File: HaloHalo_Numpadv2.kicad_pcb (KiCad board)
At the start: 2 copper layers, 112 x 105.4 mm, 92 parts, among them SW1 SW_SPST, SW10 SW_SPST, SW11 SW_SPST, SW12 SW_SPST, SW13 SW_SPST, SW14 SW_SPST, SW15 SW_SPST, SW16 SW_SPST, SW17 SW_SPST, SW18 SW_SPST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

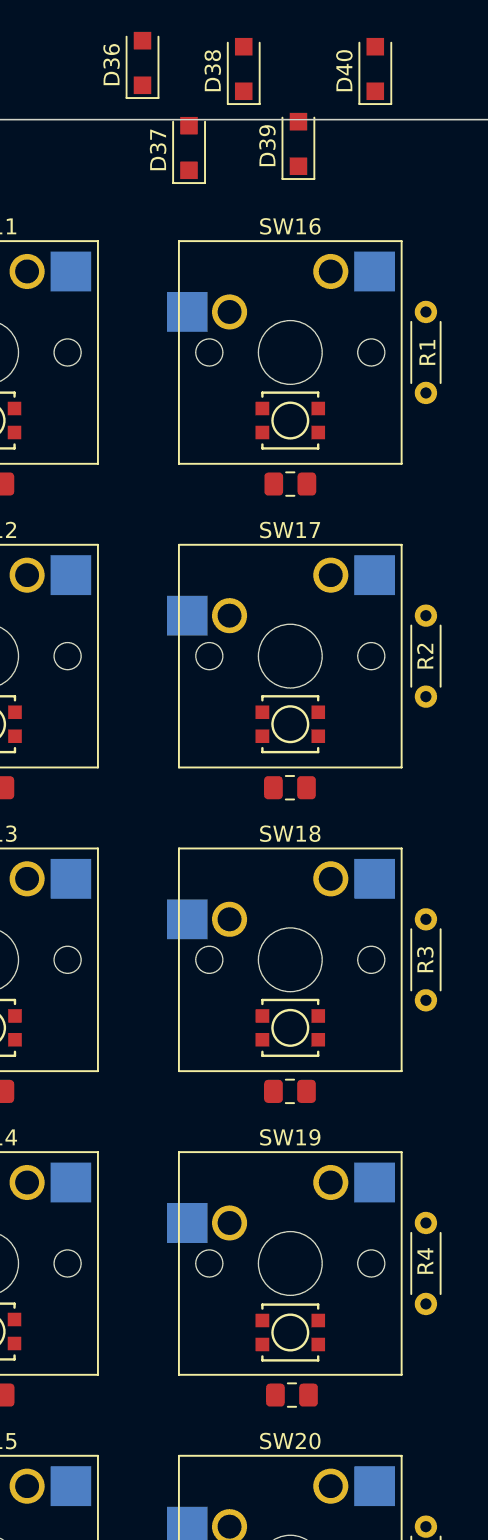
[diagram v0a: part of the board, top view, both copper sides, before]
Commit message: Changed colors of PCB assembly files in Board2Pdf. Placed all diodes on PCB.
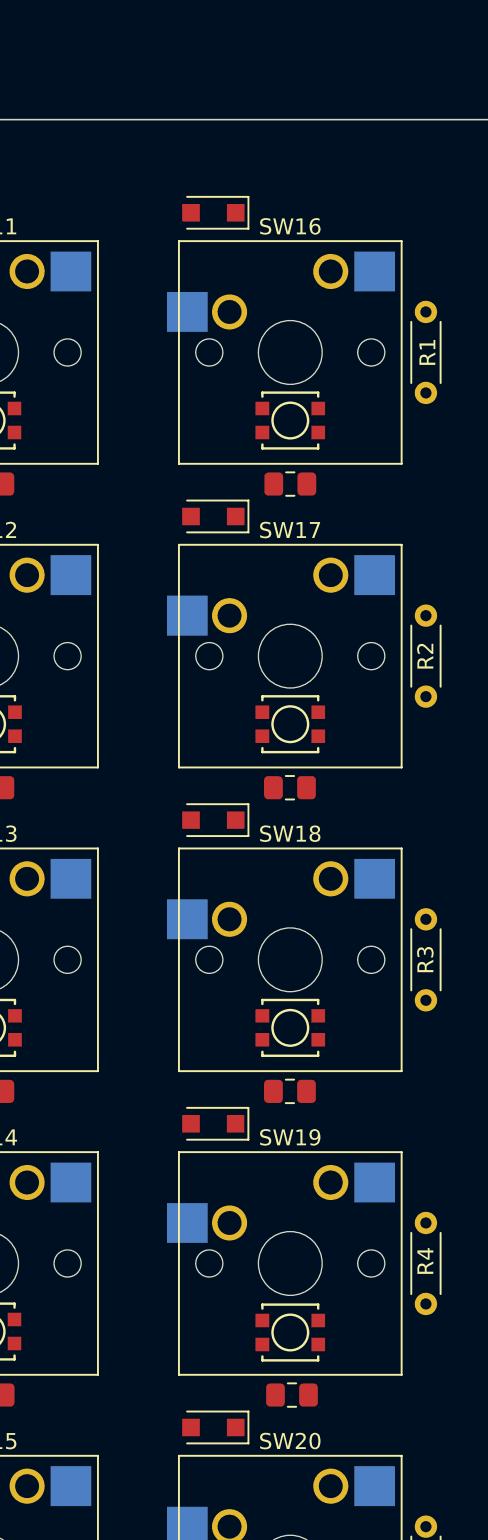
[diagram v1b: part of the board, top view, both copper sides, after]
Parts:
- moved D40 85.8 mm to (175.4, 127.3), turned to 180 degrees
- moved D39 61.7 mm to (175.4, 108.2), turned to 180 degrees
- moved D38 47.2 mm to (175.4, 89.2), turned to 180 degrees
- moved D37 23.2 mm to (175.4, 70.1), turned to 180 degrees
- moved D36 10.4 mm to (175.4, 51.1), turned to 180 degrees
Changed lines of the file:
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@@
   )
   (footprint "Diode_SMD:D_SOD-123F" (layer "F.Cu")
-    (at 170.942 41.656 90)
+    (at 175.387 51.054 180)
     (descr "D_SOD-123F")
     (tags "D_SOD-123F")
@@
     (property "Sheetname" "")
     (attr smd)
-    (fp_text reference "D36" (at -0.127 -1.905 90) (layer "F.SilkS")
-      (effects (font (size 1 1) (thickness 0.15)))
-    )
-    (fp_text value "D" (at 0 2.1 90) (layer "F.Fab")
-      (effects (font (size 1 1) (thickness 0.15)))
-    )
-    (fp_text user "${REFERENCE}" (at -0.127 -1.905 90) (layer "F.Fab")
+    (fp_text reference "D36" (at -0.127 1.905) (layer "F.Fab")
+      (effects (font (size 1 1) (thickness 0.15)))
+    )
+    (fp_text value "D" (at 0 2.1) (layer "F.Fab") hide
+      (effects (font (size 1 1) (thickness 0.15)))
+    )
+    (fp_text user "${REFERENCE}" (at -0.127 1.905) (layer "F.Fab")
       (effects (font (size 1 1) (thickness 0.15)))
     )
@@
     (fp_line (start 0.25 0) (end 0.75 0) (layer "F.Fab") (width 0.1))
     (fp_line (start 1.4 -0.9) (end 1.4 0.9) (layer "F.Fab") (width 0.1))
-    (pad "1" smd rect locked (at -1.4 0 90) (size 1.1 1.1) (layers "F.Cu" "F.Paste" "F.Mask")
+    (pad "1" smd rect locked (at -1.4 0 180) (size 1.1 1.1) (layers "F.Cu" "F.Paste" "F.Mask")
       (net 47 "Net-(D36-Pad1)") (pinfunction "K") (pintype "passive"))
-    (pad "2" smd rect locked (at 1.4 0 90) (size 1.1 1.1) (layers "F.Cu" "F.Paste" "F.Mask")
+    (pad "2" smd rect locked (at 1.4 0 180) (size 1.1 1.1) (layers "F.Cu" "F.Paste" "F.Mask")
       (net 31 "C4") (pinfunction "A") (pintype "passive"))
     (model "${KICAD6_3DMODEL_DIR}/Diode_SMD.3dshapes/D_SOD-123F.wrl"
@@
   )
   (footprint "Diode_SMD:D_SOD-123F" (layer "F.Cu")
-    (at 180.721 46.736 90)
+    (at 175.384 108.204 180)
     (descr "D_SOD-123F")
     (tags "D_SOD-123F")
@@
     (property "Sheetname" "")
     (attr smd)
-    (fp_text reference "D39" (at -0.127 -1.905 90) (layer "F.SilkS")
-      (effects (font (size 1 1) (thickness 0.15)))
-    )
-    (fp_text value "D" (at 0 2.1 90) (layer "F.Fab")
-      (effects (font (size 1 1) (thickness 0.15)))
-    )
-    (fp_text user "${REFERENCE}" (at -0.127 -1.905 90) (layer "F.Fab")
+    (fp_text reference "D39" (at -0.13 2.032) (layer "F.Fab")
+      (effects (font (size 1 1) (thickness 0.15)))
+    )
+    (fp_text value "D" (at 0 2.1) (layer "F.Fab") hide
+      (effects (font (size 1 1) (thickness 0.15)))
+    )
+    (fp_text user "${REFERENCE}" (at -0.13 2.032) (layer "F.Fab")
       (effects (font (size 1 1) (thickness 0.15)))
     )
@@
     (fp_line (start 1.4 0.9) (end -1.4 0.9) (layer "F.Fab") (width 0.1))
     (fp_line (start -0.35 0) (end 0.25 -0.4) (layer "F.Fab") (width 0.1))
-    (pad "1" smd rect locked (at -1.4 0 90) (size 1.1 1.1) (layers "F.Cu" "F.Paste" "F.Mask")
+    (pad "1" smd rect locked (at -1.4 0 180) (size 1.1 1.1) (layers "F.Cu" "F.Paste" "F.Mask")
       (net 50 "Net-(D39-Pad1)") (pinfunction "K") (pintype "passive"))
-    (pad "2" smd rect locked (at 1.4 0 90) (size 1.1 1.1) (layers "F.Cu" "F.Paste" "F.Mask")
+    (pad "2" smd rect locked (at 1.4 0 180) (size 1.1 1.1) (layers "F.Cu" "F.Paste" "F.Mask")
       (net 31 "C4") (pinfunction "A") (pintype "passive"))
     (model "${KICAD6_3DMODEL_DIR}/Diode_SMD.3dshapes/D_SOD-123F.wrl"
@@
   )
   (footprint "Diode_SMD:D_SOD-123F" (layer "F.Cu")
-    (at 177.292 42.034 90)
+    (at 175.387 89.154 180)
     (descr "D_SOD-123F")
     (tags "D_SOD-123F")
@@
     (property "Sheetname" "")
     (attr smd)
-    (fp_text reference "D38" (at -0.127 -1.905 90) (layer "F.SilkS")
-      (effects (font (size 1 1) (thickness 0.15)))
-    )
-    (fp_text value "D" (at 0 2.1 90) (layer "F.Fab")
-      (effects (font (size 1 1) (thickness 0.15)))
-    )
-    (fp_text user "${REFERENCE}" (at -0.127 -1.905 90) (layer "F.Fab")
+    (fp_text reference "D38" (at -0.127 1.905) (layer "F.Fab")
+      (effects (font (size 1 1) (thickness 0.15)))
+    )
+    (fp_text value "D" (at 0 2.1) (layer "F.Fab") hide
+      (effects (font (size 1 1) (thickness 0.15)))
+    )
+    (fp_text user "${REFERENCE}" (at -0.127 1.905) (layer "F.Fab")
       (effects (font (size 1 1) (thickness 0.15)))
     )
@@
     (fp_line (start 1.4 0.9) (end -1.4 0.9) (layer "F.Fab") (width 0.1))
     (fp_line (start -0.35 0) (end -0.35 0.55) (layer "F.Fab") (width 0.1))
-    (pad "1" smd rect locked (at -1.4 0 90) (size 1.1 1.1) (layers "F.Cu" "F.Paste" "F.Mask")
+    (pad "1" smd rect locked (at -1.4 0 180) (size 1.1 1.1) (layers "F.Cu" "F.Paste" "F.Mask")
       (net 49 "Net-(D38-Pad1)") (pinfunction "K") (pintype "passive"))
-    (pad "2" smd rect locked (at 1.4 0 90) (size 1.1 1.1) (layers "F.Cu" "F.Paste" "F.Mask")
+    (pad "2" smd rect locked (at 1.4 0 180) (size 1.1 1.1) (layers "F.Cu" "F.Paste" "F.Mask")
       (net 31 "C4") (pinfunction "A") (pintype "passive"))
     (model "${KICAD6_3DMODEL_DIR}/Diode_SMD.3dshapes/D_SOD-123F.wrl"
@@
   )
   (footprint "Diode_SMD:D_SOD-123F" (layer "F.Cu")
-    (at 173.863 46.99 90)
+    (at 175.387 70.104 180)
     (descr "D_SOD-123F")
     (tags "D_SOD-123F")
@@
     (property "Sheetname" "")
     (attr smd)
-    (fp_text reference "D37" (at -0.127 -1.905 90) (layer "F.SilkS")
-      (effects (font (size 1 1) (thickness 0.15)))
-    )
-    (fp_text value "D" (at 0 2.1 90) (layer "F.Fab")
-      (effects (font (size 1 1) (thickness 0.15)))
-    )
-    (fp_text user "${REFERENCE}" (at -0.127 -1.905 90) (layer "F.Fab")
+    (fp_text reference "D37" (at -0.254 1.905) (layer "F.Fab")
+      (effects (font (size 1 1) (thickness 0.15)))
+    )
+    (fp_text value "D" (at 0 2.1) (layer "F.Fab") hide
+      (effects (font (size 1 1) (thickness 0.15)))
+    )
+    (fp_text user "${REFERENCE}" (at -0.254 1.905) (layer "F.Fab")
       (effects (font (size 1 1) (thickness 0.15)))
     )
@@
     (fp_line (start 1.4 0.9) (end -1.4 0.9) (layer "F.Fab") (width 0.1))
     (fp_line (start -0.35 0) (end 0.25 -0.4) (layer "F.Fab") (width 0.1))
-    (pad "1" smd rect locked (at -1.4 0 90) (size 1.1 1.1) (layers "F.Cu" "F.Paste" "F.Mask")
+    (pad "1" smd rect locked (at -1.4 0 180) (size 1.1 1.1) (layers "F.Cu" "F.Paste" "F.Mask")
       (net 48 "Net-(D37-Pad1)") (pinfunction "K") (pintype "passive"))
-    (pad "2" smd rect locked (at 1.4 0 90) (size 1.1 1.1) (layers "F.Cu" "F.Paste" "F.Mask")
+    (pad "2" smd rect locked (at 1.4 0 180) (size 1.1 1.1) (layers "F.Cu" "F.Paste" "F.Mask")
       (net 31 "C4") (pinfunction "A") (pintype "passive"))
     (model "${KICAD6_3DMODEL_DIR}/Diode_SMD.3dshapes/D_SOD-123F.wrl"
@@
   )
   (footprint "Diode_SMD:D_SOD-123F" (layer "F.Cu")
-    (at 185.547 42.034 90)
+    (at 175.387 127.254 180)
     (descr "D_SOD-123F")
     (tags "D_SOD-123F")
@@
     (property "Sheetname" "")
     (attr smd)
-    (fp_text reference "D40" (at -0.127 -1.905 90) (layer "F.SilkS")
-      (effects (font (size 1 1) (thickness 0.15)))
-    )
-    (fp_text value "D" (at 0 2.1 90) (layer "F.Fab")
-      (effects (font (size 1 1) (thickness 0.15)))
-    )
-    (fp_text user "${REFERENCE}" (at -0.127 -1.905 90) (layer "F.Fab")
+    (fp_text reference "D40" (at -0.127 1.905) (layer "F.Fab")
+      (effects (font (size 1 1) (thickness 0.15)))
+    )
+    (fp_text value "D" (at 0 2.1) (layer "F.Fab") hide
+      (effects (font (size 1 1) (thickness 0.15)))
+    )
+    (fp_text user "${REFERENCE}" (at -0.127 1.905) (layer "F.Fab")
       (effects (font (size 1 1) (thickness 0.15)))
     )
@@
     (fp_line (start 1.4 -0.9) (end 1.4 0.9) (layer "F.Fab") (width 0.1))
     (fp_line (start -0.35 0) (end -0.35 -0.55) (layer "F.Fab") (width 0.1))
-    (pad "1" smd rect locked (at -1.4 0 90) (size 1.1 1.1) (layers "F.Cu" "F.Paste" "F.Mask")
+    (pad "1" smd rect locked (at -1.4 0 180) (size 1.1 1.1) (layers "F.Cu" "F.Paste" "F.Mask")
       (net 51 "Net-(D40-Pad1)") (pinfunction "K") (pintype "passive"))
-    (pad "2" smd rect locked (at 1.4 0 90) (size 1.1 1.1) (layers "F.Cu" "F.Paste" "F.Mask")
+    (pad "2" smd rect locked (at 1.4 0 180) (size 1.1 1.1) (layers "F.Cu" "F.Paste" "F.Mask")
       (net 31 "C4") (pinfunction "A") (pintype "passive"))
     (model "${KICAD6_3DMODEL_DIR}/Diode_SMD.3dshapes/D_SOD-123F.wrl"

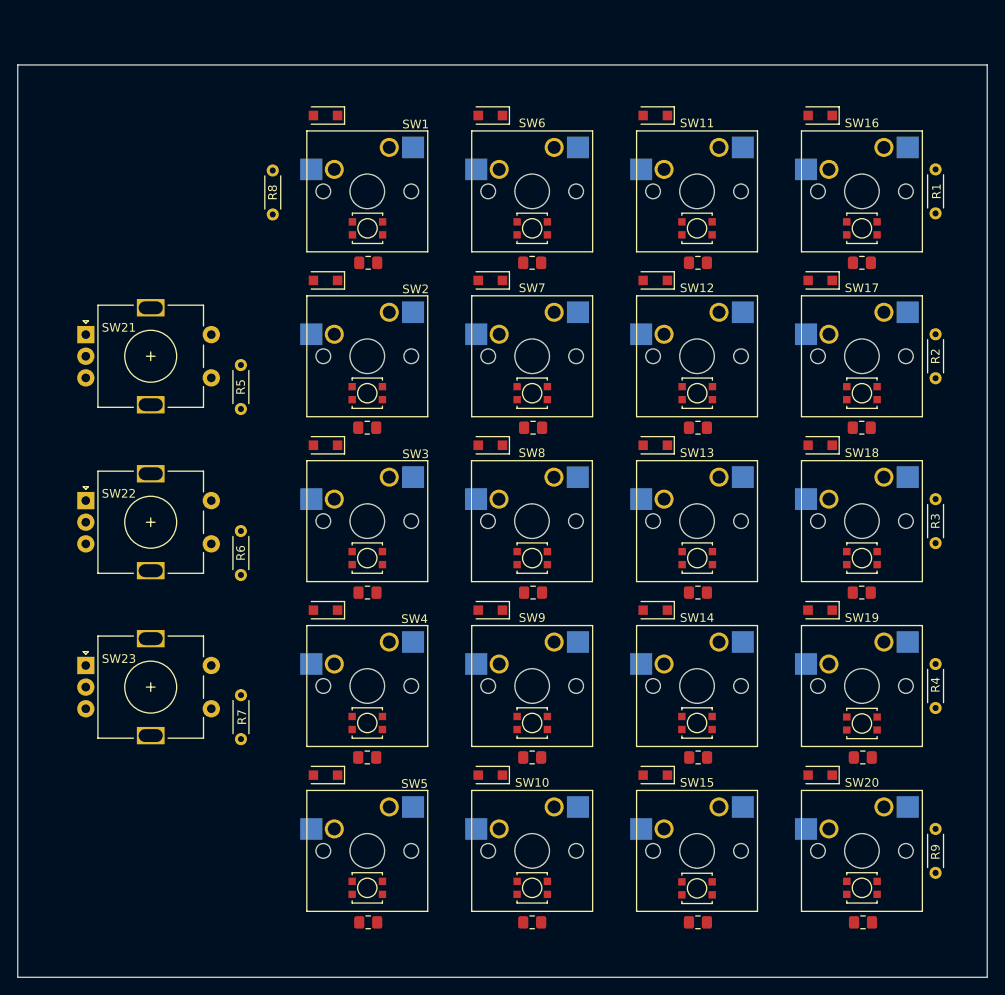
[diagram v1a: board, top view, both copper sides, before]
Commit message: Flipped orientation of key switches. Began initial trace routing.
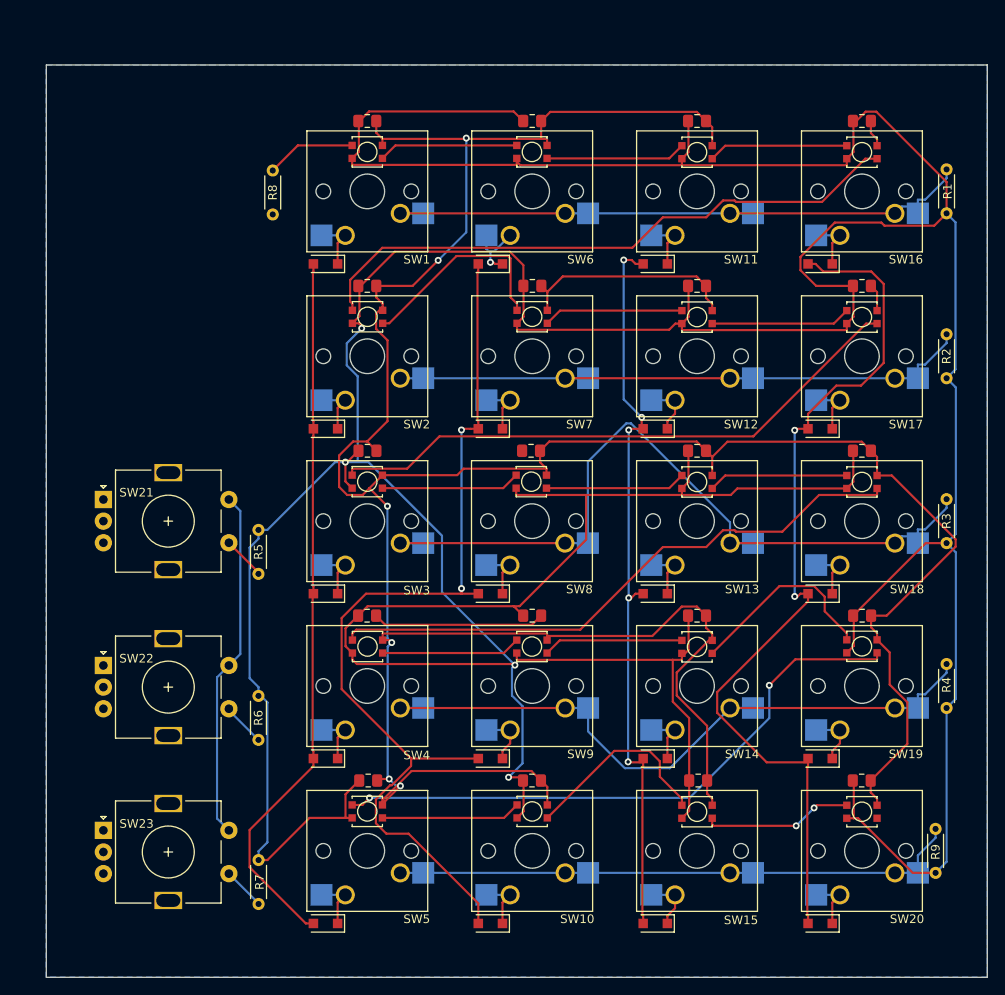
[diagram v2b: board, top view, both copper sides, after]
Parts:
- moved R5 19.2 mm to (110.5, 104.0)
- moved SW23 19.2 mm to (92.6, 133.6)
- moved R6 19.2 mm to (110.5, 123.2)
- moved R7 19.2 mm to (110.5, 142.2)
- moved SW21 19.2 mm to (92.6, 95.4)
- moved SW22 19.2 mm to (92.6, 114.6)
- moved D33 17.1 mm to (156.3, 106.3)
- moved D39 17.1 mm to (175.4, 125.3)
- moved D26 17.1 mm to (137.3, 68.2)
- moved D30 17.1 mm to (137.3, 144.4)
- moved D23 17.1 mm to (118.2, 106.3)
- moved D24 17.1 mm to (118.2, 125.3)
- moved D28 17.1 mm to (137.3, 106.3)
- moved D29 17.1 mm to (137.3, 125.3)
- moved D34 17.1 mm to (156.3, 125.3)
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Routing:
- net VCC: track 0.00 -> 644.6 mm, vias 0 -> 4
- net GNDD: track 0.00 -> 412.6 mm, vias 0 -> 6
- net C2: track 0.00 -> 111.6 mm, vias 0 -> 2
- net C4: track 0.00 -> 104.3 mm, vias 0 -> 2
- net R3: track 0.00 -> 90.7 mm
- net C3: track 0.00 -> 85.7 mm, vias 0 -> 5
- net C1: track 0.00 -> 83.4 mm
- net R4: track 0.00 -> 79.4 mm
- net R1: track 0.00 -> 72.4 mm
- net Net-(D19-Pad2): track 0.00 -> 70.6 mm, vias 0 -> 2
- net Net-(D16-Pad2): track 0.00 -> 70.4 mm
- net R2: track 0.00 -> 69.4 mm
- net Net-(D18-Pad2): track 0.00 -> 68.9 mm
- net Net-(D17-Pad2): track 0.00 -> 68.3 mm
- net R5: track 0.00 -> 65.7 mm
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- added copper zone on B.Cu, net GND
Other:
- board size 112 x 105.4 mm -> 108.7 x 105.4 mm
